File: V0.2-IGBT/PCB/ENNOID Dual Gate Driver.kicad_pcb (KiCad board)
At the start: 2 copper layers, 60 x 98 mm, 135 parts, among them J1 Conn_02x08_Odd_Even, J2 Current, J3 TEMP, J4 PHASE, J5 Collector, J6 Gate_H, J7 G_L, J8 E, Q3 MJD44H11RLG, Q4 MJD45H11RLG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

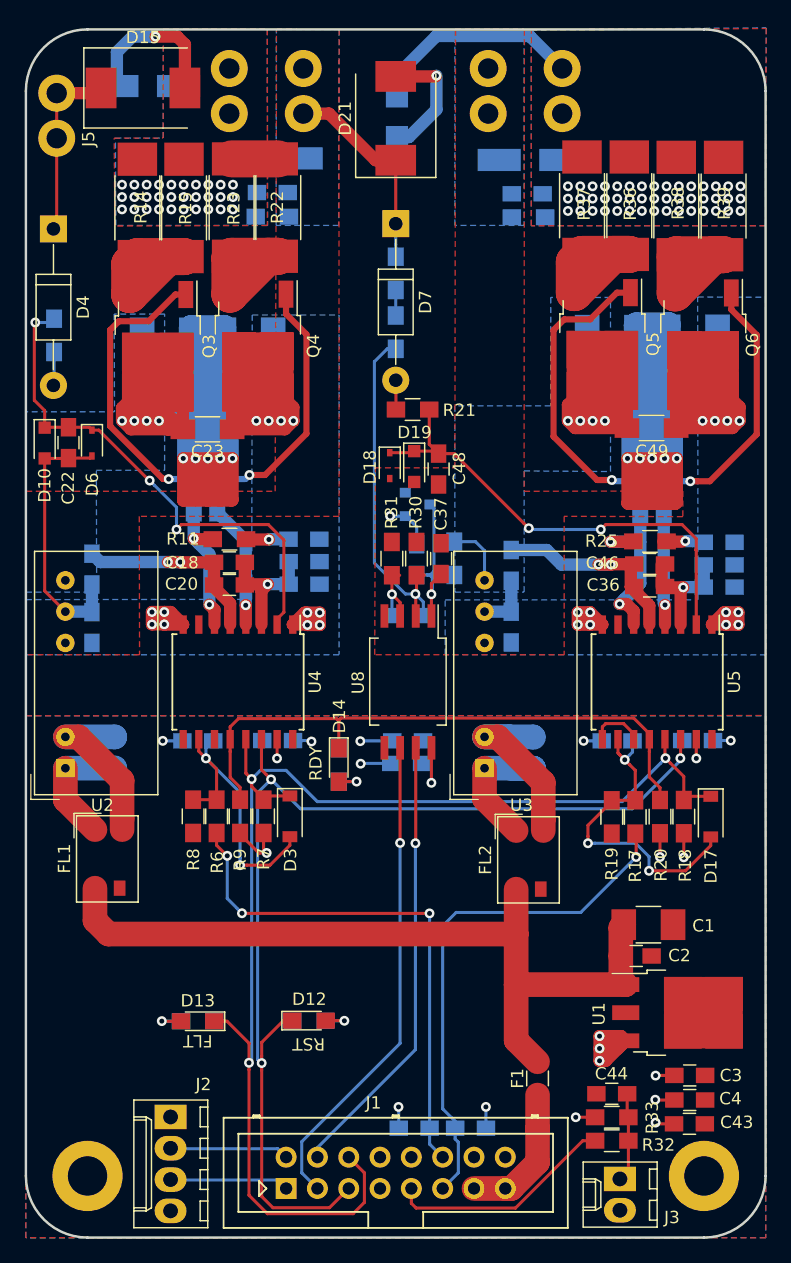
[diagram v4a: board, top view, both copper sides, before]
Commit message: V0.2 shoot through EMI protection added
In response to Marcos repply to my post on endless sphere https://endless-sphere.com/forums/viewtopic.php?f=30&t=89056&start=75
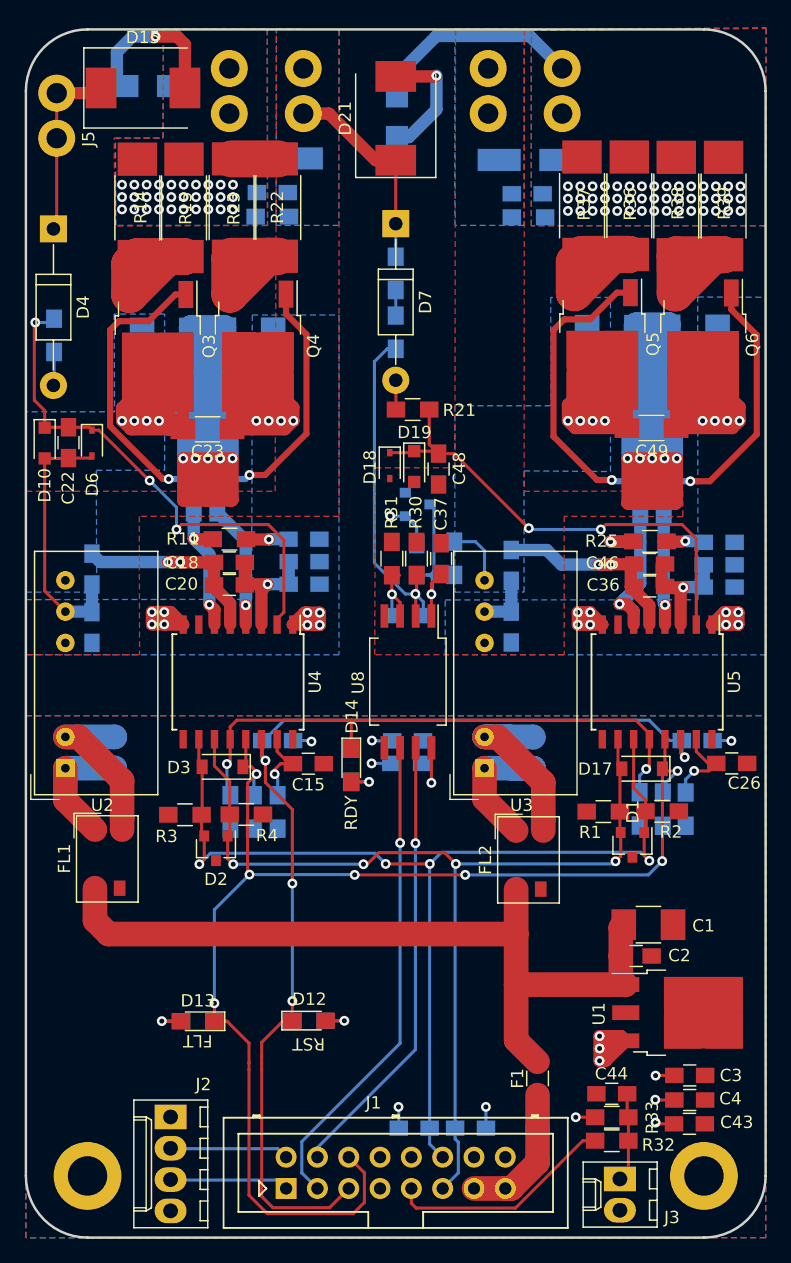
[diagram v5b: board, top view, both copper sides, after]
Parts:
- removed C27: 100n, Capacitors_SMD:C_0805_HandSoldering
- removed R17: 1k, Resistors_SMD:R_0805_HandSoldering
- removed R19: 47k, Resistors_SMD:R_0805_HandSoldering
- removed the REF** at (55.0, 93.0)
- removed the REF** at (5.00, 93.0)
- added C14: 100n, Capacitors_SMD:C_0805_HandSoldering, B.Cu at (54.5, 57.7)
- added D1: GSOT03C, TO_SOT_Packages_SMD:SOT-23, F.Cu at (49.2, 66.1)
- added D2: GSOT03C, TO_SOT_Packages_SMD:SOT-23, F.Cu at (15.4, 66.4)
- added R1: 4.7k, Resistors_SMD:R_0805_HandSoldering, F.Cu at (46.8, 63.4)
- added R2: 1k, Resistors_SMD:R_0805_HandSoldering, F.Cu at (51.6, 63.4)
- added R3: 4.7k, Resistors_SMD:R_0805_HandSoldering, F.Cu at (12.9, 63.7)
- added R4: 1k, Resistors_SMD:R_0805_HandSoldering, F.Cu at (17.9, 63.7)
- added REF**: MountingHole_3.2mm_M3_ISO14580_Pad, Mounting_Holes:MountingHole_3.2mm_M3_ISO14580_Pad, F.Cu at (55.0, 93.0)
- added REF**: MountingHole_3.2mm_M3_ISO14580_Pad, Mounting_Holes:MountingHole_3.2mm_M3_ISO14580_Pad, F.Cu at (5.00, 93.0)
- C15, C26: moved to F.Cu
- R18, R20, R7, R9: moved to B.Cu
- R6: value 1k -> 10; moved to B.Cu
- R8: value 47k -> 10; moved to B.Cu
- moved R8 40.0 mm to (53.5, 63.2), turned to 270 degrees
- moved C26 9.47 mm to (57.3, 59.5)
- moved C15 9.16 mm to (22.9, 59.6)
- moved D17 6.79 mm to (50.0, 60.0), turned to 180 degrees
- moved D3 6.78 mm to (16.0, 59.8), turned to 180 degrees
- moved R6 4.97 mm to (20.4, 63.5)
- moved R18 1.81 mm to (51.7, 63.2)
- moved R20 1.77 mm to (49.8, 63.2)
- moved G*** 1.50 mm to (30.0, 74.0)
- moved D14 1.02 mm to (26.4, 59.7)
- moved R34 1.02 mm to (26.4, 59.7)
- moved R7 0.86 mm to (18.5, 63.5)
- moved R9 0.86 mm to (16.6, 63.5)
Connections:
- C15 pad 1: Net-(C15-Pad1) -> GND
- C15 pad 2: GND -> Net-(C15-Pad2)
- C16 pad 1: +5V -> RST
- C26 pad 1: Net-(C26-Pad1) -> GND
- C26 pad 2: GND -> Net-(C26-Pad2)
- D17 pad 2: Net-(C26-Pad1) -> PWM_L
- D3 pad 2: Net-(C15-Pad1) -> PWM_H
- R6 pad 1: Net-(C15-Pad1) -> Net-(C15-Pad2)
- R6 pad 2: PWM_H -> +5V
- R8 pad 1: GND -> Net-(C26-Pad2)
- R8 pad 2: Net-(C15-Pad1) -> +5V
- U4 pad 10: Net-(C15-Pad1) -> PWM_H
- U4 pad 11: GND -> PWM_L
- U4 pad 15: +5V -> Net-(C15-Pad2)
- U5 pad 10: Net-(C26-Pad1) -> PWM_L
- U5 pad 11: GND -> PWM_H
- U5 pad 15: +5V -> Net-(C26-Pad2)
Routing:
- net PWM_H: track 43.0 -> 83.3 mm, vias 3 -> 4
- net PWM_L: track 42.3 -> 80.6 mm, vias 1 -> 4
- net Net-(C26-Pad1): track 26.8 -> 0.00 mm, vias 3 -> 0
- net Net-(C15-Pad1): track 24.3 -> 0.00 mm, vias 2 -> 0
- net +5V: track 30.2 -> 18.5 mm, vias 13 -> 8
- net GND: track 19.0 -> 9.77 mm, vias 8 -> 6
- net Net-(C26-Pad2): track 0.00 -> 7.83 mm, vias 0 -> 1
- net Net-(C15-Pad2): track 0.00 -> 6.55 mm, vias 0 -> 1
- net RDY: track 49.2 -> 47.8 mm, vias 0 -> 2
- net RST: track 89.5 -> 88.8 mm, vias 3 -> 4
- net FLT: track 106.0 -> 105.6 mm, vias 3 -> 7
